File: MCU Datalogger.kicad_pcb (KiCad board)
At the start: 2 copper layers, 0 parts

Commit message: Setup PCBnew
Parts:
- added BT1: Battery, Connector_PinHeader_2.54mm:PinHeader_1x02_P2.54mm_Vertical, F.Cu at (103.9, 83.0)
- added C1: 0.1uF, Capacitor_SMD:C_0805_2012Metric, F.Cu at (126.2, 73.1)
- added C2: 22pF, Capacitor_SMD:C_0805_2012Metric, F.Cu at (126.2, 76.1)
- added C3: 22pF, Capacitor_SMD:C_0805_2012Metric, F.Cu at (126.2, 79.1)
- added C4: 0.1uF, Capacitor_SMD:C_0805_2012Metric, F.Cu at (126.2, 82.1)
- added C5: 100nF, Capacitor_SMD:C_0805_2012Metric, F.Cu at (126.2, 85.1)
- added D1: LED, LED_SMD:LED_0805_2012Metric, F.Cu at (130.7, 73.1)
- added D2: LED, LED_SMD:LED_0805_2012Metric, F.Cu at (130.7, 76.1)
- added H1: MountingHole, MountingHole:MountingHole_2.1mm, F.Cu at (104.5, 60.5)
- added H2: MountingHole, MountingHole:MountingHole_2.1mm, F.Cu at (104.5, 66.3)
- added H3: MountingHole, MountingHole:MountingHole_2.1mm, F.Cu at (104.5, 72.0)
- added H4: MountingHole, MountingHole:MountingHole_2.1mm, F.Cu at (104.5, 77.8)
- added J1: Conn_01x04_Pin, Connector_PinHeader_2.54mm:PinHeader_1x04_P2.54mm_Vertical, F.Cu at (141.8, 60.0)
- added J2: Conn_01x09_Pin, Connector_PinHeader_2.54mm:PinHeader_1x09_P2.54mm_Vertical, F.Cu at (137.2, 60.0)
- added J3: Conn_01x04_Pin, Connector_PinHeader_2.54mm:PinHeader_1x04_P2.54mm_Vertical, F.Cu at (146.4, 60.0)
- added J4: Conn_02x03_Odd_Even, Connector_PinHeader_2.54mm:PinHeader_2x03_P2.54mm_Vertical, F.Cu at (141.8, 72.2)
- added R1: 10K, Resistor_SMD:R_0805_2012Metric, F.Cu at (109.6, 59.1)
- added R2: 10K, Resistor_SMD:R_0805_2012Metric, F.Cu at (109.6, 62.1)
- added R3: 4.7K, Resistor_SMD:R_0805_2012Metric, F.Cu at (109.6, 65.0)
- added R4: 4.7K, Resistor_SMD:R_0805_2012Metric, F.Cu at (109.6, 68.0)
- added R5: 330, Resistor_SMD:R_0805_2012Metric, F.Cu at (109.6, 70.9)
- added R6: 10K, Resistor_SMD:R_0805_2012Metric, F.Cu at (109.6, 73.9)
- added R7: 330, Resistor_SMD:R_0805_2012Metric, F.Cu at (109.6, 76.8)
- added U1: 24LC1025, Package_SO:SOIC-8_5.3x5.3mm_P1.27mm, F.Cu at (116.9, 61.2)
- added U2: 24LC1025, Package_SO:SOIC-8_5.3x5.3mm_P1.27mm, F.Cu at (116.9, 68.2)
- added U3: DS1337S_, DS1337S_:SOIC127P600X175-8N, F.Cu at (116.9, 86.2)
- added U4: ATMEGA328P-AU, ATMEGA328P-AU:QFP80P900X900X120-32N, F.Cu at (118.3, 77.3)
- added Y1: 32.768 KHz, Crystal:Crystal_SMD_5032-2Pin_5.0x3.2mm_HandSoldering, F.Cu at (127.3, 60.3)
- added Y2: 16 MHz, Crystal:Crystal_SMD_5032-2Pin_5.0x3.2mm_HandSoldering, F.Cu at (127.3, 65.5)

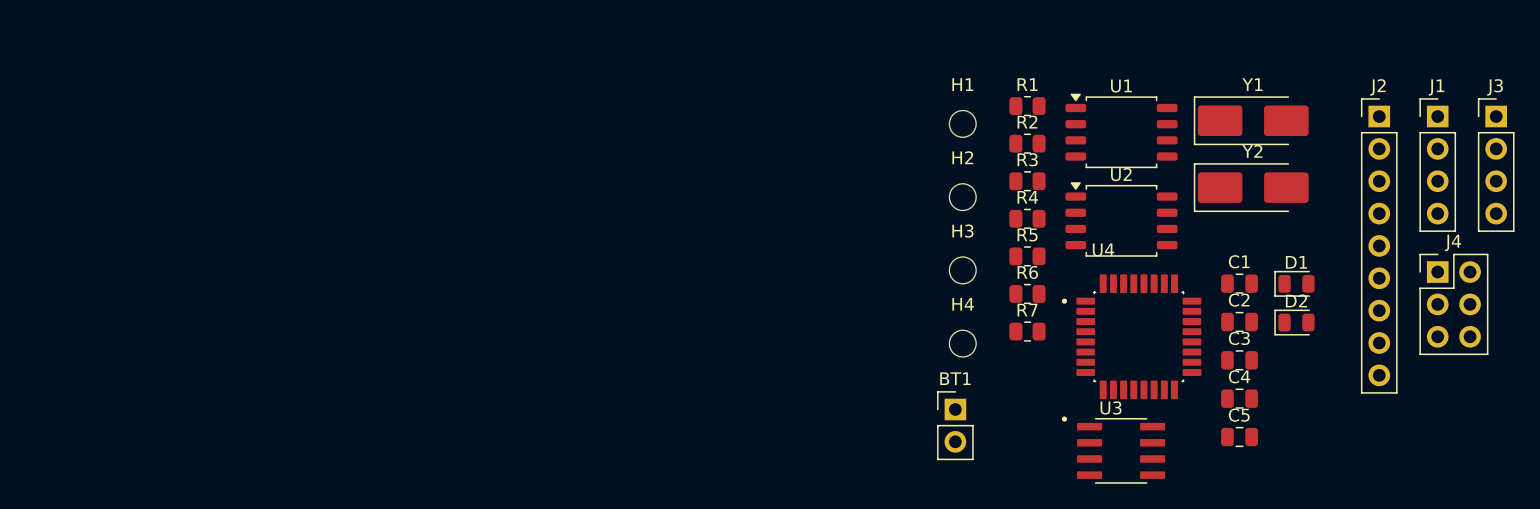
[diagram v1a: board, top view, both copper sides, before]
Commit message: Completed placement of footprints
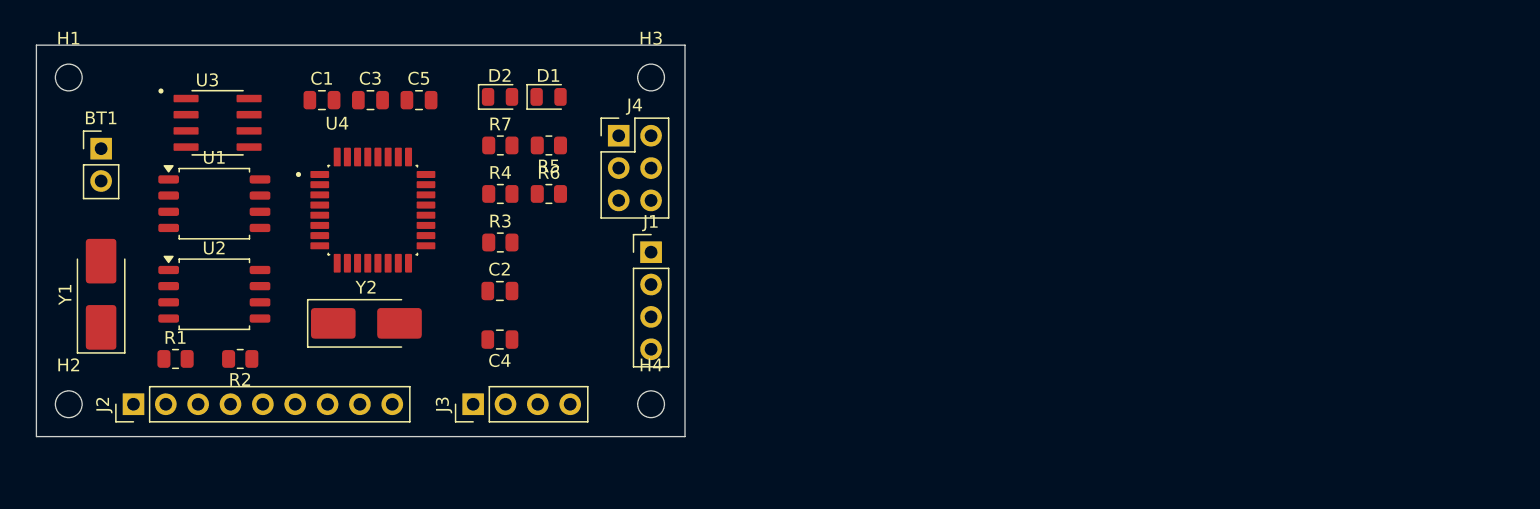
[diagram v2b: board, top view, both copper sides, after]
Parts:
- moved J2 100.4 mm to (39.4, 82.5), turned to 90 degrees
- moved Y1 91.5 mm to (36.8, 73.9), turned to 90 degrees
- moved J3 83.4 mm to (66.0, 82.5), turned to 90 degrees
- moved U3 75.5 mm to (46.0, 60.5)
- moved C1 73.5 mm to (54.2, 58.7)
- moved H2 72.1 mm to (34.3, 82.5)
- moved U2 71.5 mm to (45.7, 73.9)
- moved U1 71.4 mm to (45.7, 66.8)
- moved C3 71.2 mm to (58.0, 58.7)
- moved Y2 70.4 mm to (57.7, 76.2)
- moved H1 70.3 mm to (34.3, 56.9)
- moved BT1 70.1 mm to (36.8, 62.5)
- moved R1 69.8 mm to (42.7, 79.0)
- moved C5 69.6 mm to (61.8, 58.7)
- moved J4 65.2 mm to (77.5, 61.5)
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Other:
- board outline added: 50.9 x 30.7 mm

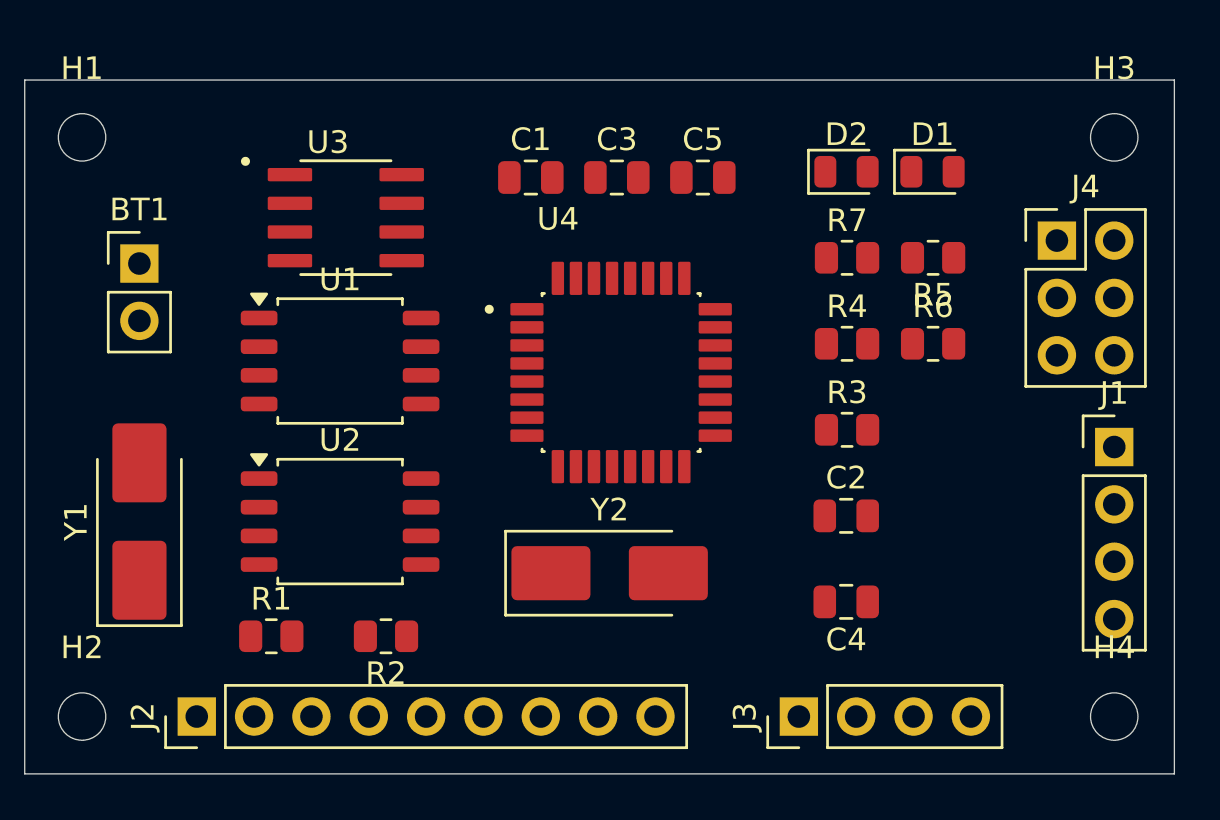
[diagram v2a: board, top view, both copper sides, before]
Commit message: Partial routing in front and back layers
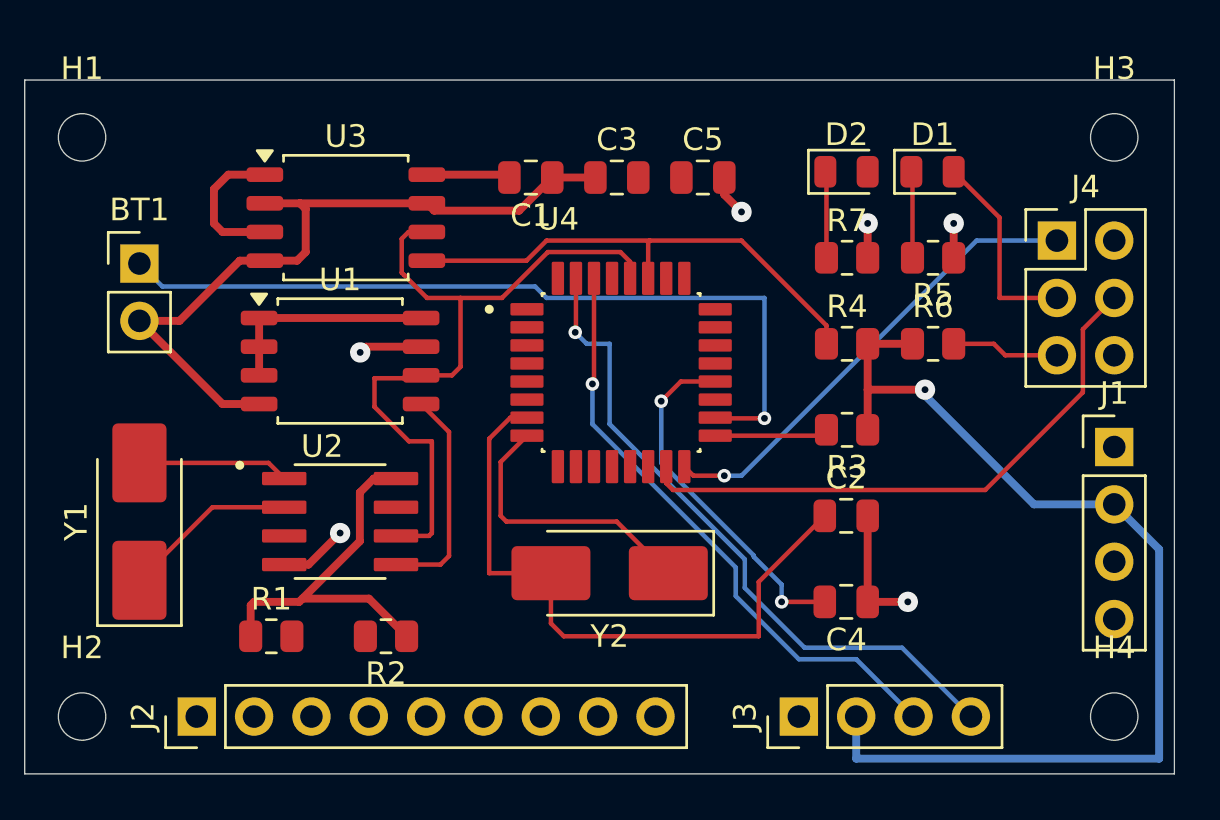
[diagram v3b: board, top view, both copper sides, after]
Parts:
- U2: value 24LC1025 -> DS1337S_; footprint Package_SO:SOIC-8_5.3x5.3mm_P1.27mm -> DS1337S_:SOIC127P600X175-8N
- U3: value DS1337S_ -> 24LC1025; footprint DS1337S_:SOIC127P600X175-8N -> Package_SO:SOIC-8_5.3x5.3mm_P1.27mm
- turned C1 to 180 degrees
- turned R3 to 180 degrees
- turned Y2 to 180 degrees
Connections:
- R1 pad 2: Net-(U3-~{INTA}) -> Net-(U2-~{INTA})
- R2 pad 2: Net-(U3-SQW/~INT) -> Net-(U2-SQW/~INT)
- U2 pad 1: /VCC -> Net-(U2-X1)
- U2 pad 2: GND -> Net-(U2-X2)
- U2 pad 3: /VCC -> Net-(U2-~{INTA})
- U2 pad 7: GND -> Net-(U2-SQW/~INT)
- U3 pad 1: Net-(U3-X1) -> /VCC
- U3 pad 2: Net-(U3-X2) -> GND
- U3 pad 3: Net-(U3-~{INTA}) -> /VCC
- U3 pad 7: Net-(U3-SQW/~INT) -> GND
- Y1 pad 1: Net-(U3-X2) -> Net-(U2-X2)
- Y1 pad 2: Net-(U3-X1) -> Net-(U2-X1)
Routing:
- net /VCC: track 0.00 -> 82.9 mm, vias 0 -> 1
- net GND: track 0.00 -> 49.9 mm, vias 0 -> 6
- net /SCK: track 0.00 -> 46.3 mm
- net Net-(BT1-+): track 0.00 -> 35.8 mm, vias 0 -> 1
- net /SDA: track 0.00 -> 31.9 mm
- net /TX: track 0.00 -> 29.8 mm, vias 0 -> 1
- net Net-(U4-PB6): track 0.00 -> 29.0 mm
- net /RX: track 0.00 -> 26.8 mm, vias 0 -> 1
- net /MOSI: track 0.00 -> 25.9 mm
- net /MISO: track 0.00 -> 21.0 mm, vias 0 -> 1
- net Net-(U4-AREF): track 0.00 -> 15.8 mm, vias 0 -> 2
- net Net-(U4-PB7): track 0.00 -> 12.5 mm
- net Net-(U2-X2): track 0.00 -> 7.75 mm
- net Net-(U2-X1): track 0.00 -> 6.70 mm
- net /RESET: track 0.00 -> 4.78 mm
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
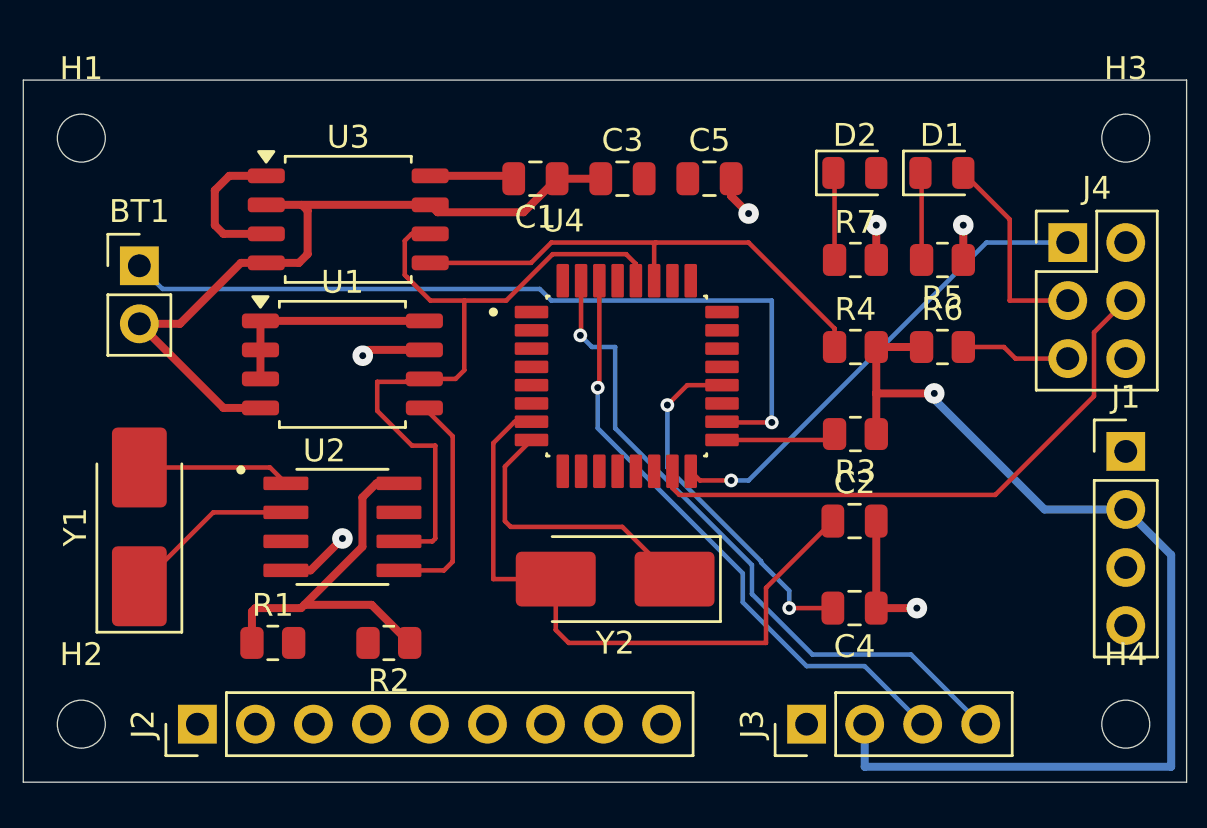
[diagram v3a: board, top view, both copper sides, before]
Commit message: Routing completed (except GND and VCC)
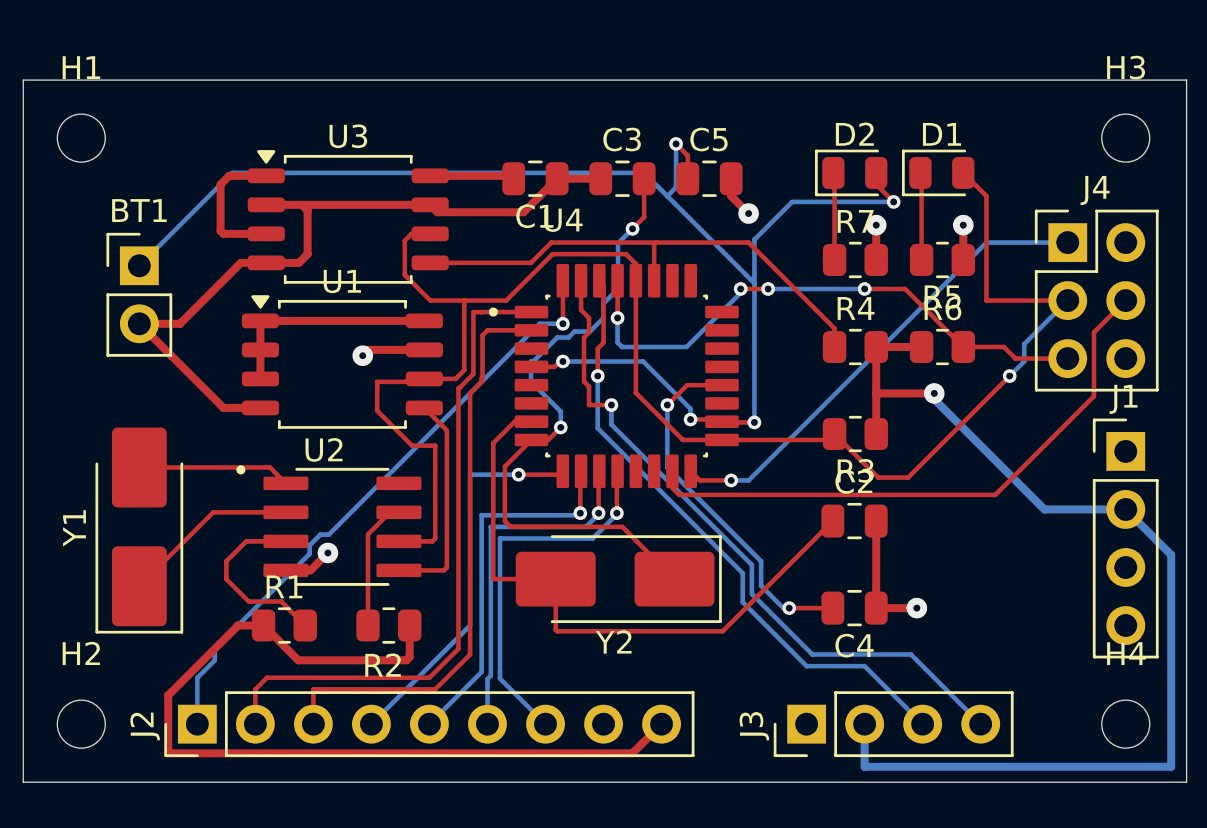
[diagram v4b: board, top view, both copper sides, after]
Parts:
- moved R1 0.92 mm to (43.2, 78.2)
- moved R2 0.76 mm to (47.8, 78.2)
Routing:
- net /D3: track 0.00 -> 28.7 mm
- net /D2: track 0.00 -> 26.9 mm, vias 0 -> 1
- net Net-(BT1-+): track 35.8 -> 62.4 mm, vias 1 -> 5
- net /D4: track 0.00 -> 25.4 mm
- net /SCK: track 46.3 -> 71.1 mm, vias 0 -> 1
- net /VCC: track 82.9 -> 104.6 mm
- net /RESET: track 4.78 -> 24.9 mm, vias 0 -> 4
- net /D5: track 0.00 -> 16.8 mm, vias 0 -> 1
- net /D8: track 0.00 -> 16.4 mm, vias 0 -> 1
- net /D6: track 0.00 -> 16.3 mm, vias 0 -> 1
- net Net-(U4-PB7): track 12.5 -> 28.2 mm, vias 0 -> 2
- net /D7: track 0.00 -> 15.5 mm, vias 0 -> 1
- net Net-(U2-~{INTA}): track 0.00 -> 8.04 mm
- net Net-(U2-SQW/~INT): track 0.00 -> 5.74 mm
- net Net-(U4-PB6): track 29.0 -> 27.1 mm
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
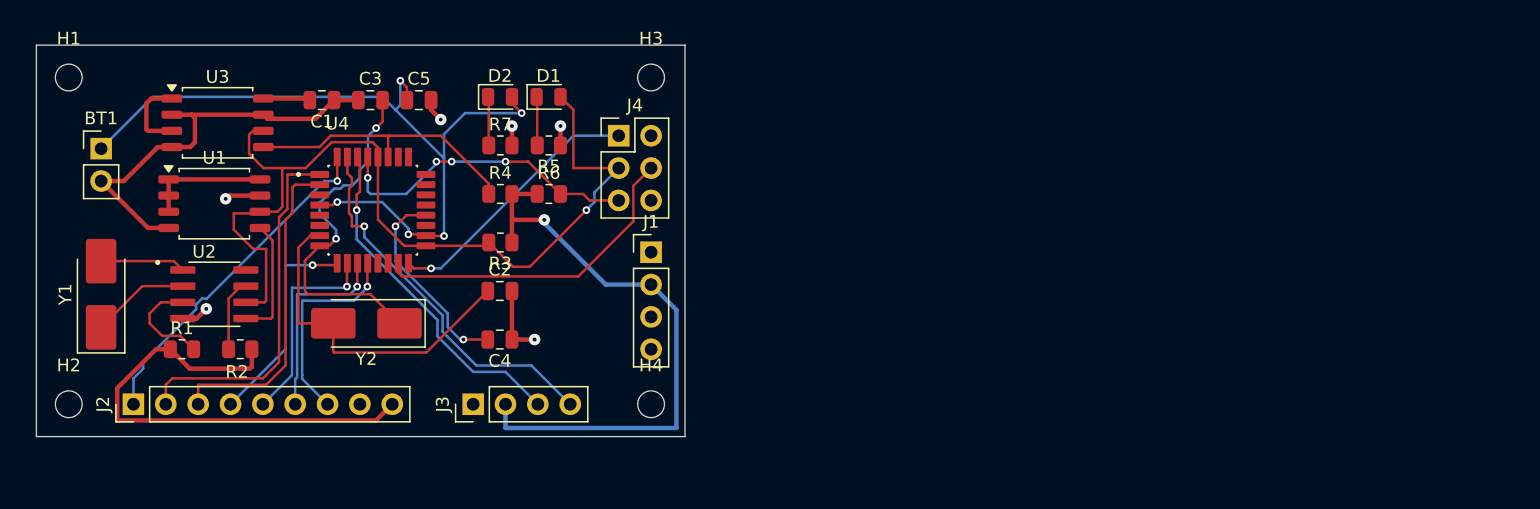
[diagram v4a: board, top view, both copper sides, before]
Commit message: Completed routing
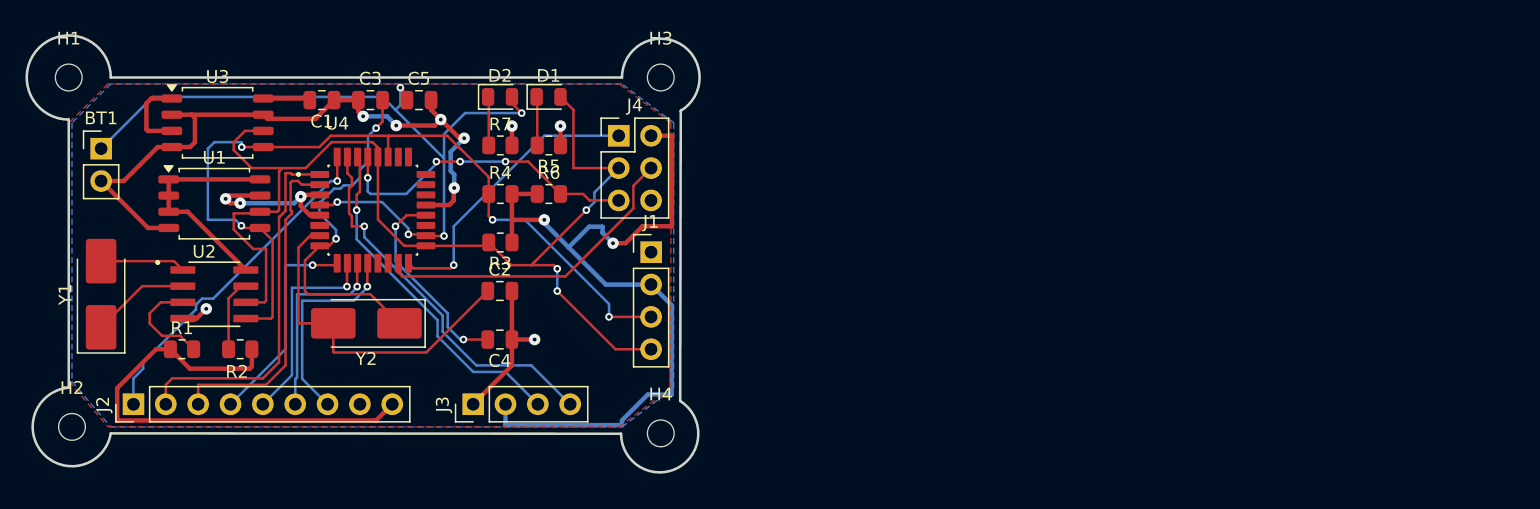
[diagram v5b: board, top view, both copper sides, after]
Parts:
- moved H4 2.41 mm to (80.8, 84.8)
- moved H2 1.80 mm to (34.5, 84.3)
- moved H3 0.76 mm to (80.8, 56.9)
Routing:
- net GND: track 49.0 -> 83.9 mm, vias 6 -> 12
- net /SDA: track 31.7 -> 65.2 mm, vias 0 -> 4
- net /VCC: track 104.6 -> 129.3 mm, vias 1 -> 2
- net /SCK: track 71.1 -> 86.0 mm, vias 1 -> 3
- net /MISO: track 21.0 -> 22.8 mm
- net Net-(BT1-+): track 62.4 -> 61.3 mm
- net /D4: track 25.4 -> 26.1 mm
- net /MOSI: track 25.9 -> 25.3 mm
- added copper zone on F.Cu, net /VCC
- added copper zone on B.Cu, net GND
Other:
- board size 50.9 x 30.7 mm -> 52.8 x 34.3 mm

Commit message: Refined routing complete
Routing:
- net Net-(U4-PB7): track 28.2 -> 27.2 mm
- net /SCK: track 86.0 -> 85.0 mm
- net /D2: track 26.9 -> 26.0 mm
- net /SDA: track 65.2 -> 64.6 mm
- net /D4: track 26.1 -> 25.6 mm
- net GND: track 83.9 -> 83.4 mm, vias 12 -> 11
